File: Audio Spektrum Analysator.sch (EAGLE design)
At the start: 157 parts, among them IC1 LM324N, IC10 LM3914N, IC11 LM3914N, IC12 LM3914N, IC13 LM3914N, IC2 LM324N, IC3 LM324N, IC4 LM3914N, IC5 LM3914N, IC6 LM3914N, IC7 LM3914N, IC8 LM3914N, IC9 LM3914N, J2 DCJ0202, M1 ELECTRET_MICROPHON-F6050AP

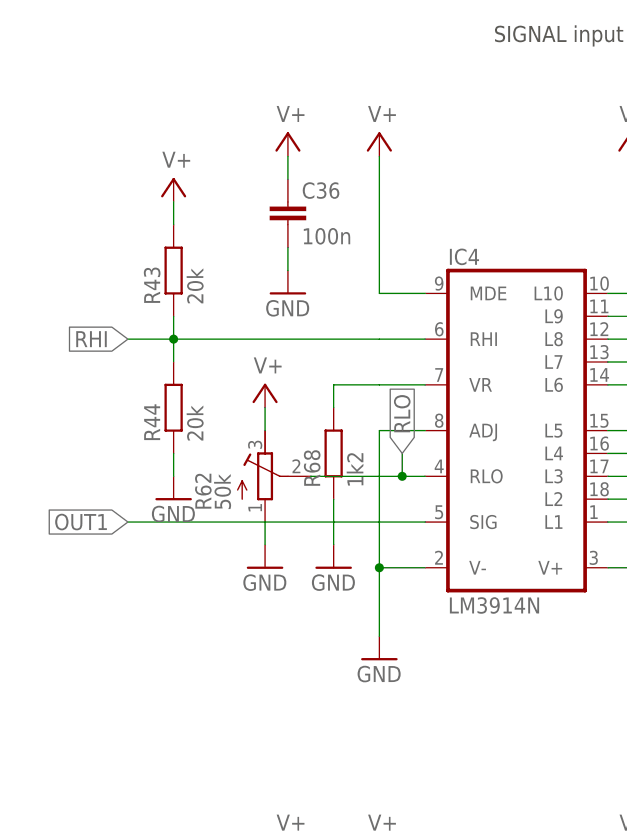
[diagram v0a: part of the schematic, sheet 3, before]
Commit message: implemented offset compensation circuit in layout
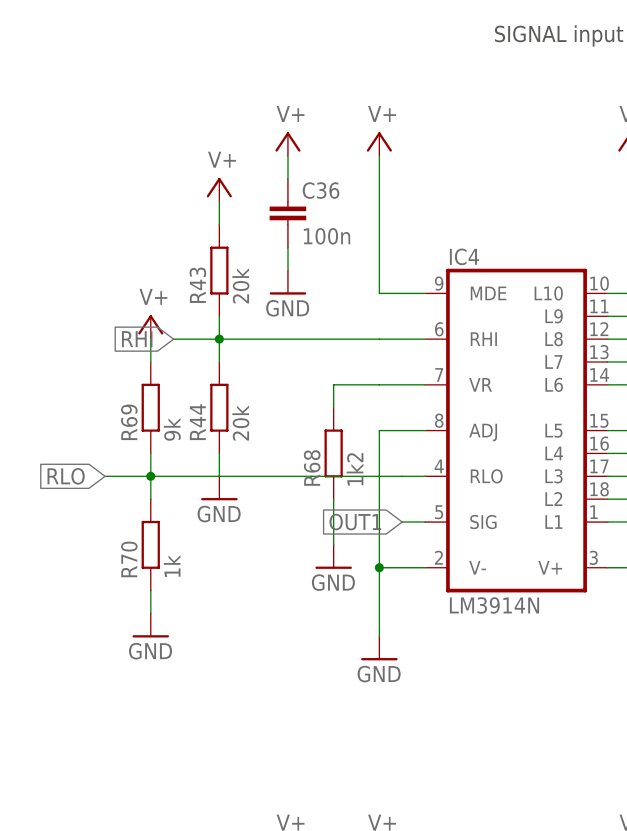
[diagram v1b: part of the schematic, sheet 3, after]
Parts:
- removed R62: 50k, resistor:R-TRIMM64W
- added R69: 9k, resistor:R-EU_0207/7
- added R70: 1k, resistor:R-EU_0207/7
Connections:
- net GND: now also R70.1; no longer R62.A
- net RLO: now also R69.1, R70.2; no longer R62.S
- net V+: now also R69.2; no longer R62.E
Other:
- moved on the sheet: R43, R44
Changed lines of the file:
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@@
 </variantdefs>
 <classes>
-<class number="0" name="default" width="0" drill="0">
+<class number="0" name="default" width="0.4064" drill="0">
+</class>
+<class number="1" name="V+" width="0.8128" drill="0">
 </class>
 </classes>
@@
 <part name="GND73" library="supply1" library_urn="urn:adsk.eagle:library:371" deviceset="GND" device=""/>
 <part name="C48" library="capacitor-wima" library_urn="urn:adsk.eagle:library:116" deviceset="C" device="5/5" package3d_urn="urn:adsk.eagle:package:5428/1" value="1u"/>
-<part name="R62" library="resistor" library_urn="urn:adsk.eagle:library:348" deviceset="R-TRIMM" device="64W" package3d_urn="urn:adsk.eagle:package:23748/1" value="50k"/>
-<part name="SUPPLY50" library="supply2" library_urn="urn:adsk.eagle:library:372" deviceset="V+" device=""/>
-<part name="GND74" library="supply1" library_urn="urn:adsk.eagle:library:371" deviceset="GND" device=""/>
+<part name="R69" library="resistor" library_urn="urn:adsk.eagle:library:348" deviceset="R-EU_" device="0207/7" package3d_urn="urn:adsk.eagle:package:23493/1" value="9k"/>
+<part name="R70" library="resistor" library_urn="urn:adsk.eagle:library:348" deviceset="R-EU_" device="0207/7" package3d_urn="urn:adsk.eagle:package:23493/1" value="1k"/>
+<part name="GND75" library="supply1" library_urn="urn:adsk.eagle:library:371" deviceset="GND" device=""/>
+<part name="SUPPLY51" library="supply2" library_urn="urn:adsk.eagle:library:372" deviceset="V+" device=""/>
 </parts>
 <sheets>
@@
 </segment>
 </net>
-<net name="V+" class="0">
+<net name="V+" class="1">
 <segment>
 <pinref part="SUPPLY1" gate="1" pin="V+"/>
@@
 <instance part="SUPPLY12" gate="1" x="81.28" y="172.72"/>
 <instance part="SUPPLY10" gate="1" x="53.34" y="172.72"/>
-<instance part="R43" gate="G$1" x="30.48" y="157.48" rot="R90"/>
-<instance part="R44" gate="G$1" x="30.48" y="142.24" rot="R90"/>
-<instance part="GND32" gate="1" x="30.48" y="132.08"/>
+<instance part="R43" gate="G$1" x="35.56" y="157.48" rot="R90"/>
+<instance part="R44" gate="G$1" x="35.56" y="142.24" rot="R90"/>
+<instance part="GND32" gate="1" x="35.56" y="132.08"/>
 <instance part="DIS3" gate="G$1" x="210.82" y="114.3"/>
 <instance part="SUPPLY22" gate="1" x="236.22" y="172.72"/>
@@
 <instance part="SUPPLY16" gate="1" x="154.94" y="172.72"/>
 <instance part="GND37" gate="1" x="154.94" y="154.94"/>
-<instance part="SUPPLY49" gate="1" x="30.48" y="167.64"/>
+<instance part="SUPPLY49" gate="1" x="35.56" y="167.64"/>
 <instance part="R68" gate="G$1" x="48.26" y="137.16" rot="R90"/>
 <instance part="GND65" gate="1" x="48.26" y="124.46"/>
-<instance part="R62" gate="G$1" x="40.64" y="134.62"/>
-<instance part="SUPPLY50" gate="1" x="40.64" y="144.78"/>
-<instance part="GND74" gate="1" x="40.64" y="124.46"/>
+<instance part="R69" gate="G$1" x="27.94" y="142.24" rot="R90"/>
+<instance part="R70" gate="G$1" x="27.94" y="127" rot="R90"/>
+<instance part="GND75" gate="1" x="27.94" y="116.84"/>
+<instance part="SUPPLY51" gate="1" x="27.94" y="152.4"/>
 </instances>
 <busses>
@@
 <pinref part="GND32" gate="1" pin="GND"/>
 <pinref part="R44" gate="G$1" pin="1"/>
-<wire x1="30.48" y1="134.62" x2="30.48" y2="137.16" width="0.1524" layer="91"/>
+<wire x1="35.56" y1="134.62" x2="35.56" y2="137.16" width="0.1524" layer="91"/>
 </segment>
 <segment>
@@
 </segment>
 <segment>
-<pinref part="GND74" gate="1" pin="GND"/>
-<pinref part="R62" gate="G$1" pin="A"/>
-<wire x1="40.64" y1="127" x2="40.64" y2="129.54" width="0.1524" layer="91"/>
+<pinref part="GND75" gate="1" pin="GND"/>
+<pinref part="R70" gate="G$1" pin="1"/>
+<wire x1="27.94" y1="119.38" x2="27.94" y2="121.92" width="0.1524" layer="91"/>
 </segment>
 </net>
@@
 <pinref part="R44" gate="G$1" pin="2"/>
 <pinref part="R43" gate="G$1" pin="1"/>
-<wire x1="30.48" y1="152.4" x2="30.48" y2="149.86" width="0.1524" layer="91"/>
-<wire x1="30.48" y1="149.86" x2="30.48" y2="147.32" width="0.1524" layer="91"/>
-<wire x1="53.34" y1="149.86" x2="30.48" y2="149.86" width="0.1524" layer="91"/>
-<junction x="30.48" y="149.86"/>
-<wire x1="30.48" y1="149.86" x2="25.4" y2="149.86" width="0.1524" layer="91"/>
-<label x="25.4" y="149.86" size="1.778" layer="95" rot="R180" xref="yes"/>
+<wire x1="35.56" y1="152.4" x2="35.56" y2="149.86" width="0.1524" layer="91"/>
+<wire x1="35.56" y1="149.86" x2="35.56" y2="147.32" width="0.1524" layer="91"/>
+<wire x1="53.34" y1="149.86" x2="35.56" y2="149.86" width="0.1524" layer="91"/>
+<junction x="35.56" y="149.86"/>
+<wire x1="35.56" y1="149.86" x2="30.48" y2="149.86" width="0.1524" layer="91"/>
+<label x="30.48" y="149.86" size="1.778" layer="95" rot="R180" xref="yes"/>
 </segment>
 <segment>
@@
 <segment>
 <pinref part="IC4" gate="A" pin="SIG"/>
-<wire x1="58.42" y1="129.54" x2="25.4" y2="129.54" width="0.1524" layer="91"/>
-<label x="25.4" y="129.54" size="1.778" layer="95" rot="R180" xref="yes"/>
+<wire x1="58.42" y1="129.54" x2="55.88" y2="129.54" width="0.1524" layer="91"/>
+<label x="55.88" y="129.54" size="1.778" layer="95" rot="R180" xref="yes"/>
 </segment>
 </net>
@@
 </segment>
 </net>
-<net name="V+" class="0">
+<net name="V+" class="1">
 <segment>
 <pinref part="R43" gate="G$1" pin="2"/>
 <pinref part="SUPPLY49" gate="1" pin="V+"/>
-<wire x1="30.48" y1="162.56" x2="30.48" y2="165.1" width="0.1524" layer="91"/>
+<wire x1="35.56" y1="162.56" x2="35.56" y2="165.1" width="0.1524" layer="91"/>
 </segment>
 <segment>
@@
 </segment>
 <segment>
-<pinref part="SUPPLY50" gate="1" pin="V+"/>
-<pinref part="R62" gate="G$1" pin="E"/>
-<wire x1="40.64" y1="142.24" x2="40.64" y2="139.7" width="0.1524" layer="91"/>
+<pinref part="R69" gate="G$1" pin="2"/>
+<pinref part="SUPPLY51" gate="1" pin="V+"/>
+<wire x1="27.94" y1="147.32" x2="27.94" y2="149.86" width="0.1524" layer="91"/>
 </segment>
 </net>
 <net name="RLO" class="0">
 <segment>
-<pinref part="R62" gate="G$1" pin="S"/>
-<pinref part="IC4" gate="A" pin="RLO"/>
-<wire x1="45.72" y1="134.62" x2="55.88" y2="134.62" width="0.1524" layer="91"/>
-<wire x1="55.88" y1="134.62" x2="58.42" y2="134.62" width="0.1524" layer="91"/>
-<wire x1="55.88" y1="134.62" x2="55.88" y2="137.16" width="0.1524" layer="91"/>
-<junction x="55.88" y="134.62"/>
-<label x="55.88" y="137.16" size="1.778" layer="95" rot="R90" xref="yes"/>
-</segment>
-<segment>
 <pinref part="IC5" gate="A" pin="RLO"/>
 <wire x1="58.42" y1="55.88" x2="43.18" y2="55.88" width="0.1524" layer="91"/>
@@
 <label x="154.94" y="134.62" size="1.778" layer="95" rot="R180" xref="yes"/>
 </segment>
+<segment>
+<pinref part="R70" gate="G$1" pin="2"/>
+<pinref part="R69" gate="G$1" pin="1"/>
+<wire x1="27.94" y1="137.16" x2="27.94" y2="134.62" width="0.1524" layer="91"/>
+<wire x1="27.94" y1="134.62" x2="27.94" y2="132.08" width="0.1524" layer="91"/>
+<junction x="27.94" y="134.62"/>
+<pinref part="IC4" gate="A" pin="RLO"/>
+<wire x1="45.72" y1="134.62" x2="55.88" y2="134.62" width="0.1524" layer="91"/>
+<wire x1="55.88" y1="134.62" x2="58.42" y2="134.62" width="0.1524" layer="91"/>
+<wire x1="27.94" y1="134.62" x2="45.72" y2="134.62" width="0.1524" layer="91"/>
+<wire x1="27.94" y1="134.62" x2="22.86" y2="134.62" width="0.1524" layer="91"/>
+<label x="22.86" y="134.62" size="1.778" layer="95" rot="R180" xref="yes"/>
+</segment>
 </net>
 </nets>
@@
 </segment>
 </net>
-<net name="V+" class="0">
+<net name="V+" class="1">
 <segment>
 <pinref part="C40" gate="G$1" pin="1"/>
@@
 </segment>
 </net>
-<net name="V+" class="0">
+<net name="V+" class="1">
 <segment>
 <pinref part="C44" gate="G$1" pin="1"/>

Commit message: finished layout
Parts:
- removed C48: 1u, capacitor-wima:C5/5
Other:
- note removed: "consider using low leackage polypropylen capacitors"
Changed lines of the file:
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@@
 <setting verticaltext="up"/>
 </settings>
-<grid distance="0.1" unitdist="inch" unit="mm" style="lines" multiple="1" display="yes" altdistance="0.01" altunitdist="inch" altunit="inch"/>
+<grid distance="2.54" unitdist="mm" unit="mm" style="lines" multiple="1" display="yes" altdistance="0.01" altunitdist="inch" altunit="inch"/>
 <layers>
 <layer number="1" name="Top" color="4" fill="1" visible="no" active="no"/>
@@
 <part name="R60" library="rcl" library_urn="urn:adsk.eagle:library:334" deviceset="R-EU_" device="0207/7" package3d_urn="urn:adsk.eagle:package:23493/1" value="100k"/>
 <part name="GND73" library="supply1" library_urn="urn:adsk.eagle:library:371" deviceset="GND" device=""/>
-<part name="C48" library="capacitor-wima" library_urn="urn:adsk.eagle:library:116" deviceset="C" device="5/5" package3d_urn="urn:adsk.eagle:package:5428/1" value="1u"/>
 <part name="R69" library="resistor" library_urn="urn:adsk.eagle:library:348" deviceset="R-EU_" device="0207/7" package3d_urn="urn:adsk.eagle:package:23493/1" value="9k"/>
 <part name="R70" library="resistor" library_urn="urn:adsk.eagle:library:348" deviceset="R-EU_" device="0207/7" package3d_urn="urn:adsk.eagle:package:23493/1" value="1k"/>
@@
 <sheet>
 <plain>
-<text x="76.2" y="182.88" size="1.778" layer="97">consider using low leackage polypropylen capacitors</text>
 </plain>
 <instances>
@@
 <instance part="R67" gate="G$1" x="246.38" y="73.66" rot="R90"/>
 <instance part="GND64" gate="1" x="246.38" y="63.5"/>
-<instance part="C48" gate="G$1" x="160.02" y="185.42"/>
 </instances>
 <busses>

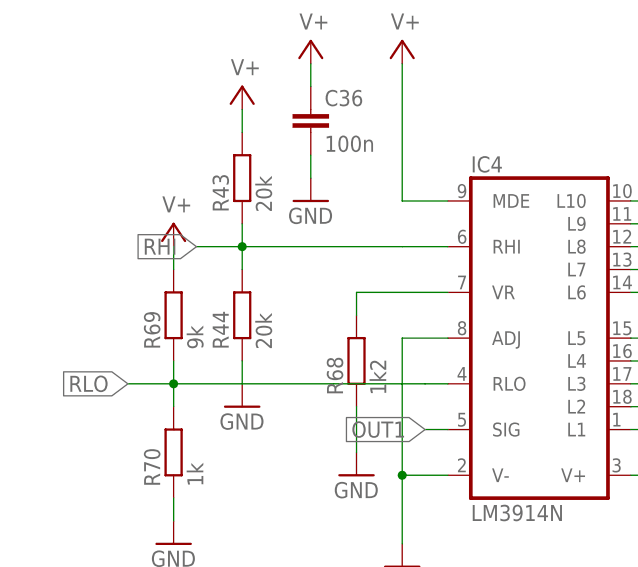
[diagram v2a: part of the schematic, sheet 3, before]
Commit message: moved names, added testpoints
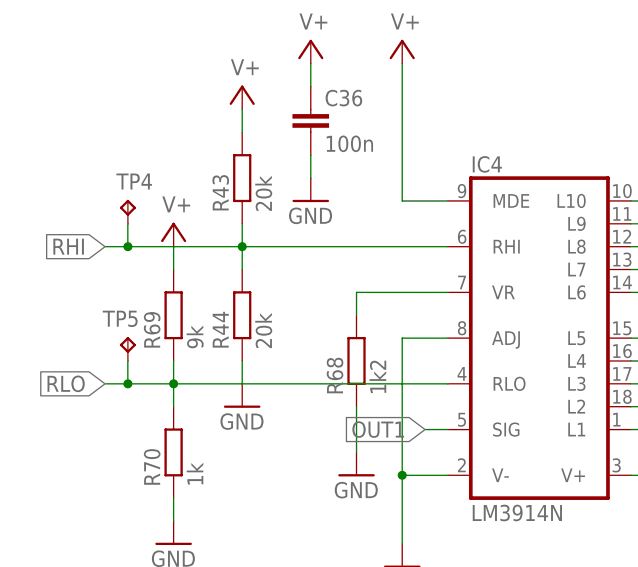
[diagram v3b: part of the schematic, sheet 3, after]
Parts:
- added TP4, TP5: TPPAD1-20, testpad:TPPAD1-20
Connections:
- net RHI: now also TP4.TP
- net RLO: now also TP5.TP
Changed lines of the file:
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@@
 <layer number="98" name="Guide" color="6" fill="1" visible="yes" active="yes"/>
 <layer number="99" name="SpiceOrder" color="7" fill="1" visible="no" active="no"/>
+<layer number="100" name="Muster" color="7" fill="1" visible="no" active="no"/>
+<layer number="113" name="ReferenceLS" color="7" fill="1" visible="no" active="no"/>
+<layer number="118" name="Rect_Pads" color="7" fill="1" visible="no" active="no"/>
+<layer number="153" name="FabDoc1" color="6" fill="1" visible="no" active="no"/>
+<layer number="154" name="FabDoc2" color="2" fill="1" visible="no" active="no"/>
+<layer number="155" name="FabDoc3" color="7" fill="15" visible="no" active="no"/>
+<layer number="217" name="217bmp" color="18" fill="1" visible="no" active="no"/>
+<layer number="218" name="218bmp" color="19" fill="1" visible="no" active="no"/>
+<layer number="219" name="219bmp" color="20" fill="1" visible="no" active="no"/>
+<layer number="220" name="220bmp" color="21" fill="1" visible="no" active="no"/>
+<layer number="221" name="221bmp" color="22" fill="1" visible="no" active="no"/>
+<layer number="222" name="222bmp" color="23" fill="1" visible="no" active="no"/>
+<layer number="223" name="223bmp" color="24" fill="1" visible="no" active="no"/>
+<layer number="224" name="224bmp" color="25" fill="1" visible="no" active="no"/>
+<layer number="231" name="Eagle3D_PG1" color="7" fill="1" visible="no" active="no"/>
+<layer number="232" name="Eagle3D_PG2" color="7" fill="1" visible="no" active="no"/>
+<layer number="233" name="Eagle3D_PG3" color="7" fill="1" visible="no" active="no"/>
+<layer number="250" name="Descript" color="3" fill="1" visible="no" active="no"/>
+<layer number="251" name="SMDround" color="12" fill="11" visible="no" active="no"/>
 </layers>
 <schematic xreflabel="%F%N/%S.%C%R" xrefpart="/%S.%C%R">
@@
 <part name="GND75" library="supply1" library_urn="urn:adsk.eagle:library:371" deviceset="GND" device=""/>
 <part name="SUPPLY51" library="supply2" library_urn="urn:adsk.eagle:library:372" deviceset="V+" device=""/>
+<part name="TP4" library="testpad" library_urn="urn:adsk.eagle:library:385" deviceset="TP" device="PAD1-20" package3d_urn="urn:adsk.eagle:package:27950/1"/>
+<part name="TP5" library="testpad" library_urn="urn:adsk.eagle:library:385" deviceset="TP" device="PAD1-20" package3d_urn="urn:adsk.eagle:package:27950/1"/>
 </parts>
 <sheets>
@@
 </segment>
 </net>
-<net name="N$137" class="0">
-<segment>
-<wire x1="27.94" y1="73.66" x2="35.56" y2="73.66" width="0.1524" layer="91"/>
-</segment>
-</net>
 <net name="N$125" class="0">
 <segment>
@@
 <instance part="GND75" gate="1" x="27.94" y="116.84"/>
 <instance part="SUPPLY51" gate="1" x="27.94" y="152.4"/>
+<instance part="TP4" gate="G$1" x="22.86" y="154.94"/>
+<instance part="TP5" gate="G$1" x="22.86" y="139.7" rot="MR0"/>
 </instances>
 <busses>
@@
 <segment>
 <pinref part="IC4" gate="A" pin="RHI"/>
-<wire x1="53.34" y1="149.86" x2="58.42" y2="149.86" width="0.1524" layer="91"/>
 <pinref part="R44" gate="G$1" pin="2"/>
 <pinref part="R43" gate="G$1" pin="1"/>
 <wire x1="35.56" y1="152.4" x2="35.56" y2="149.86" width="0.1524" layer="91"/>
 <wire x1="35.56" y1="149.86" x2="35.56" y2="147.32" width="0.1524" layer="91"/>
-<wire x1="53.34" y1="149.86" x2="35.56" y2="149.86" width="0.1524" layer="91"/>
+<wire x1="58.42" y1="149.86" x2="35.56" y2="149.86" width="0.1524" layer="91"/>
 <junction x="35.56" y="149.86"/>
-<wire x1="35.56" y1="149.86" x2="30.48" y2="149.86" width="0.1524" layer="91"/>
-<label x="30.48" y="149.86" size="1.778" layer="95" rot="R180" xref="yes"/>
+<wire x1="35.56" y1="149.86" x2="22.86" y2="149.86" width="0.1524" layer="91"/>
+<label x="20.32" y="149.86" size="1.778" layer="95" rot="R180" xref="yes"/>
+<pinref part="TP4" gate="G$1" pin="TP"/>
+<wire x1="22.86" y1="149.86" x2="20.32" y2="149.86" width="0.1524" layer="91"/>
+<wire x1="22.86" y1="152.4" x2="22.86" y2="149.86" width="0.1524" layer="91"/>
+<junction x="22.86" y="149.86"/>
 </segment>
 <segment>
@@
 <junction x="27.94" y="134.62"/>
 <pinref part="IC4" gate="A" pin="RLO"/>
-<wire x1="45.72" y1="134.62" x2="55.88" y2="134.62" width="0.1524" layer="91"/>
-<wire x1="55.88" y1="134.62" x2="58.42" y2="134.62" width="0.1524" layer="91"/>
-<wire x1="27.94" y1="134.62" x2="45.72" y2="134.62" width="0.1524" layer="91"/>
+<wire x1="27.94" y1="134.62" x2="58.42" y2="134.62" width="0.1524" layer="91"/>
 <wire x1="27.94" y1="134.62" x2="22.86" y2="134.62" width="0.1524" layer="91"/>
-<label x="22.86" y="134.62" size="1.778" layer="95" rot="R180" xref="yes"/>
-</segment>
-</net>
+<label x="20.32" y="134.62" size="1.778" layer="95" rot="R180" xref="yes"/>
+<pinref part="TP5" gate="G$1" pin="TP"/>
+<wire x1="22.86" y1="134.62" x2="20.32" y2="134.62" width="0.1524" layer="91"/>
+<wire x1="22.86" y1="137.16" x2="22.86" y2="134.62" width="0.1524" layer="91"/>
+<junction x="22.86" y="134.62"/>
+</segment>
+</net>

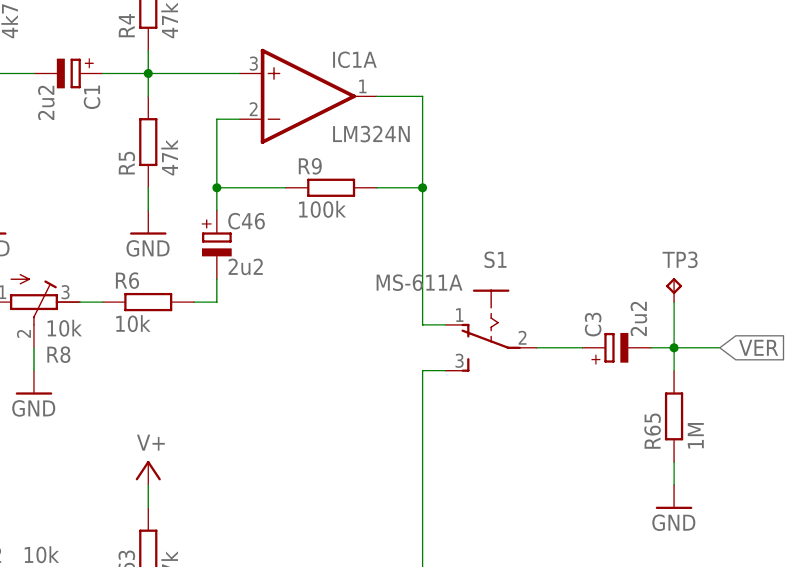
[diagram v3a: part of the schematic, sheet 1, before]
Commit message: replaced s1
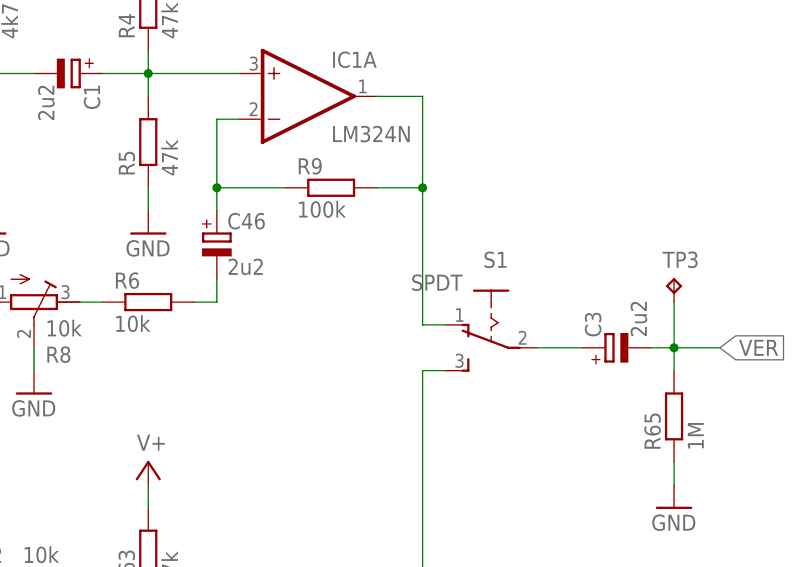
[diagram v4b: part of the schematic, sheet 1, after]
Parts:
- S1: value MS-611A -> SPDT; device 1_Robo-Lib:MS-611A -> Jakobs_LBR:SPDT
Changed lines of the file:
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@@
 <part name="SUPPLY1" library="supply2" library_urn="urn:adsk.eagle:library:372" deviceset="V+" device=""/>
 <part name="GND5" library="supply1" library_urn="urn:adsk.eagle:library:371" deviceset="GND" device=""/>
-<part name="S1" library="1_Robo-Lib" deviceset="MS-611A" device=""/>
+<part name="S1" library="Jakobs_LBR" deviceset="SPDT" device=""/>
 <part name="R6" library="rcl" library_urn="urn:adsk.eagle:library:334" deviceset="R-EU_" device="0207/7" package3d_urn="urn:adsk.eagle:package:23493/1" value="10k"/>
 <part name="TP3" library="testpad" library_urn="urn:adsk.eagle:library:385" deviceset="TP" device="PAD1-20" package3d_urn="urn:adsk.eagle:package:27950/1"/>
